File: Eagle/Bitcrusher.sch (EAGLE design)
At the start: 18 parts, among them IC1 TL074P, IC2 NE555, Q1 BF245

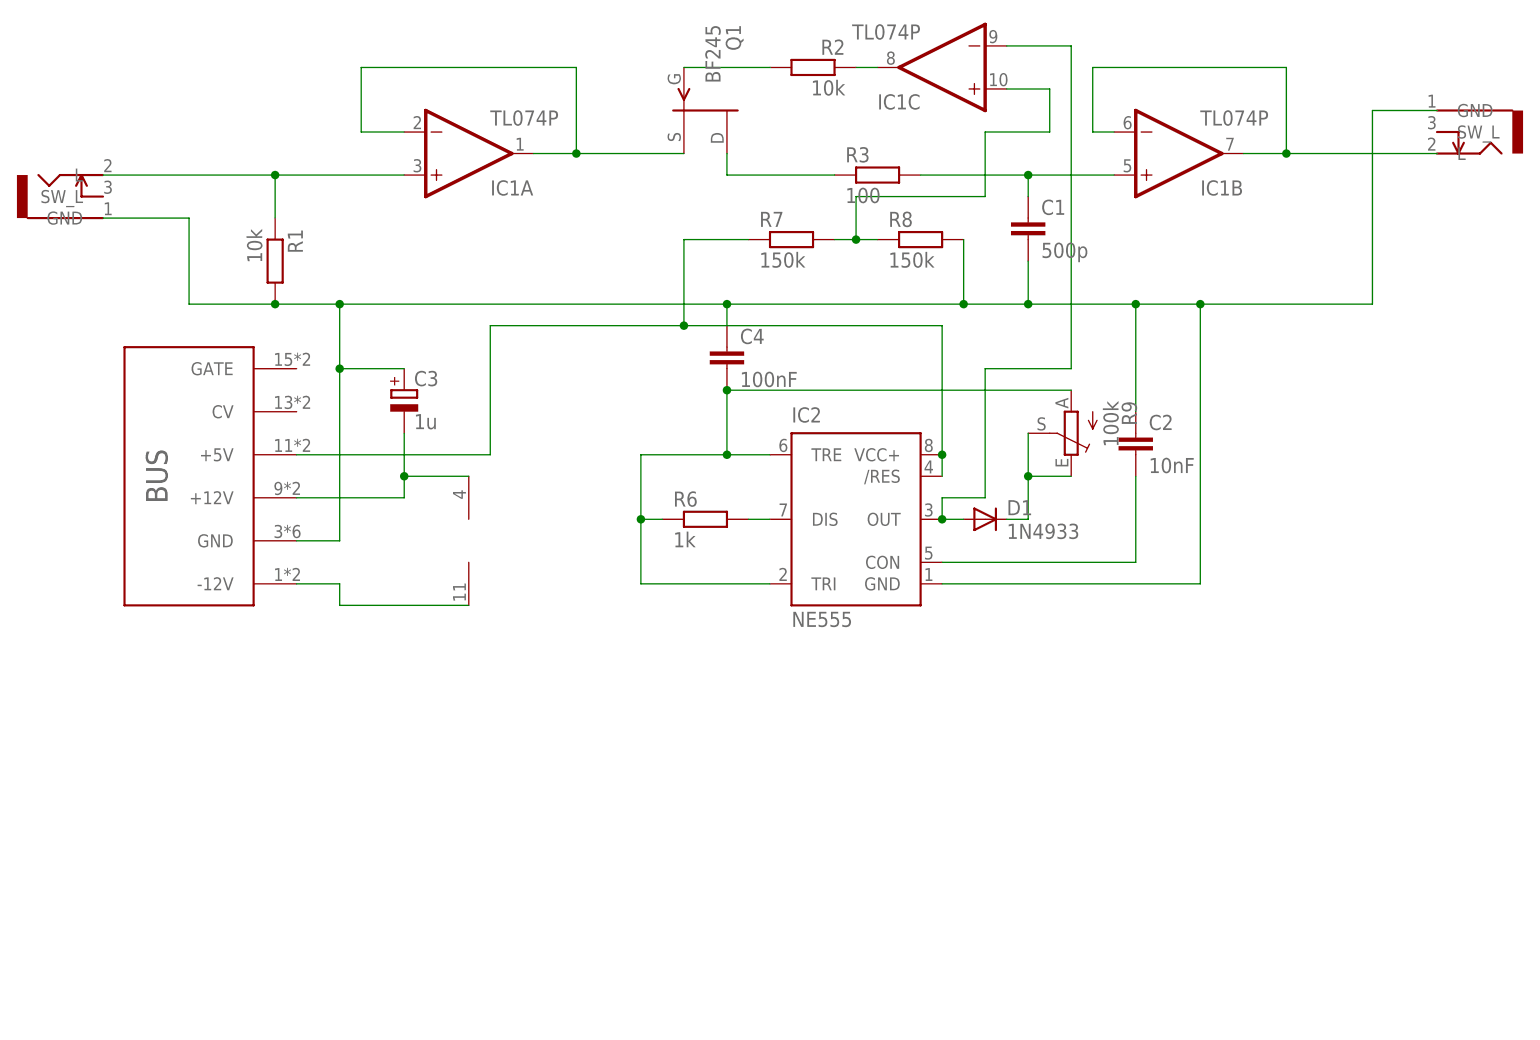
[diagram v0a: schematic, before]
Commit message: Made eagle schematic more readable.
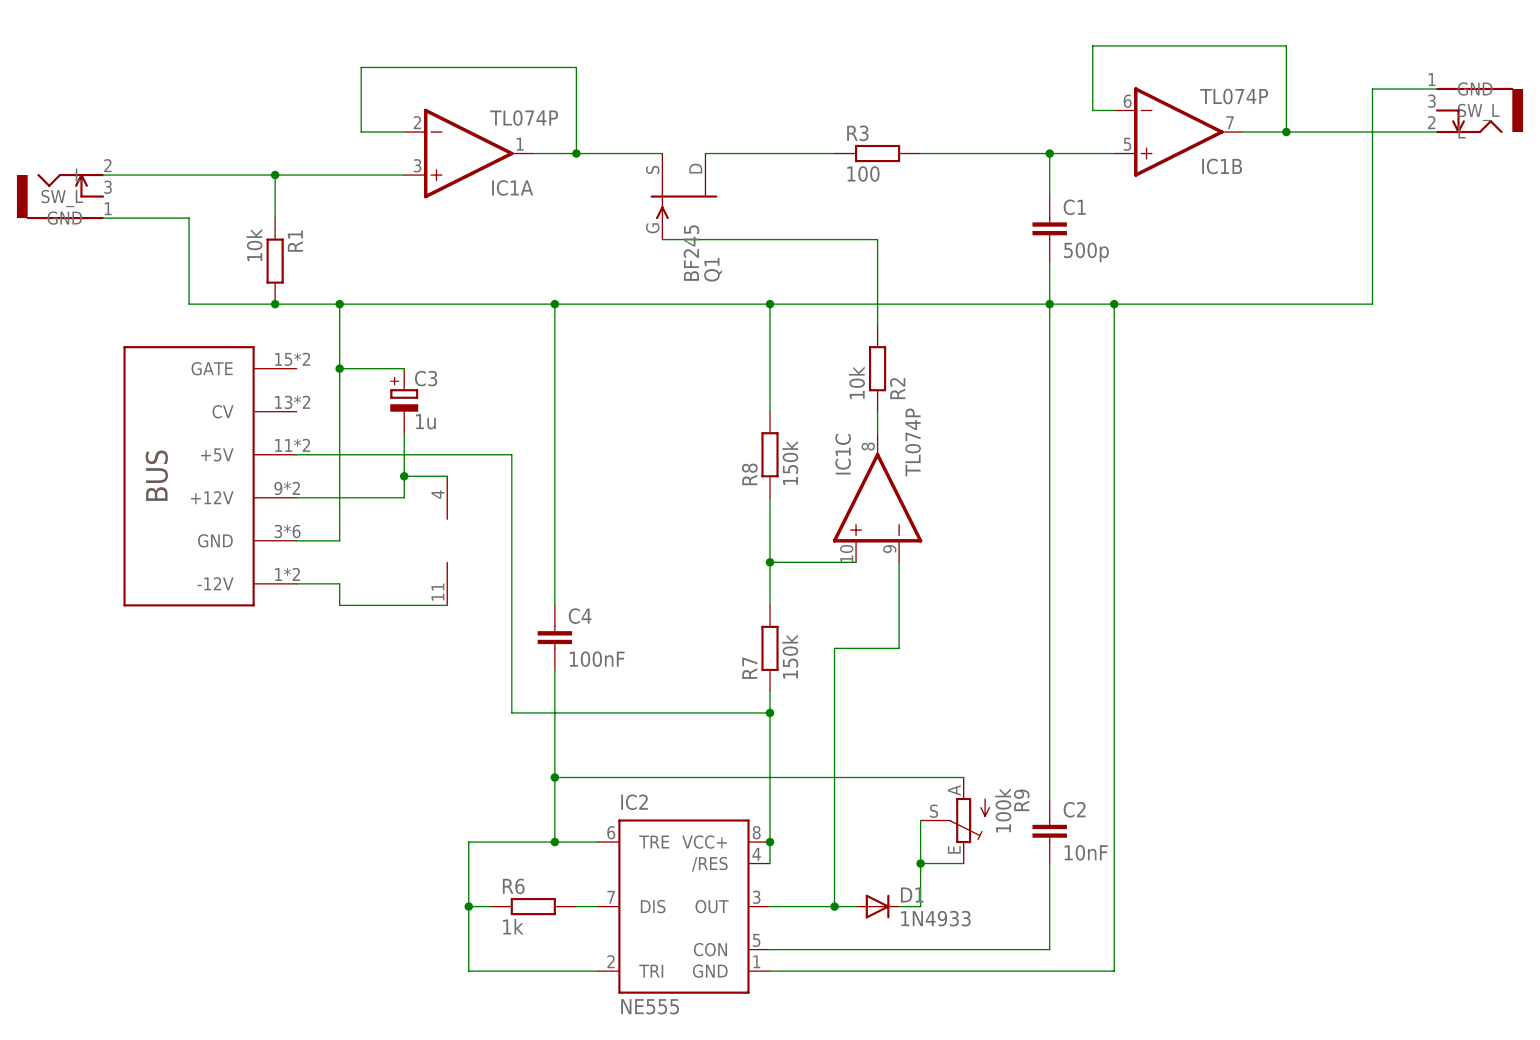
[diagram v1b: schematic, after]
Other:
- moved on the sheet: C1, C2, C4, D1, IC1B, IC1C, IC2, Q1, R2, R3, R6, R7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
